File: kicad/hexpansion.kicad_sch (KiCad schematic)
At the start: 11 parts, among them J1 Hexpansion-Connector, J2 SD Card breakout, U1 AT24CS32-SSHM

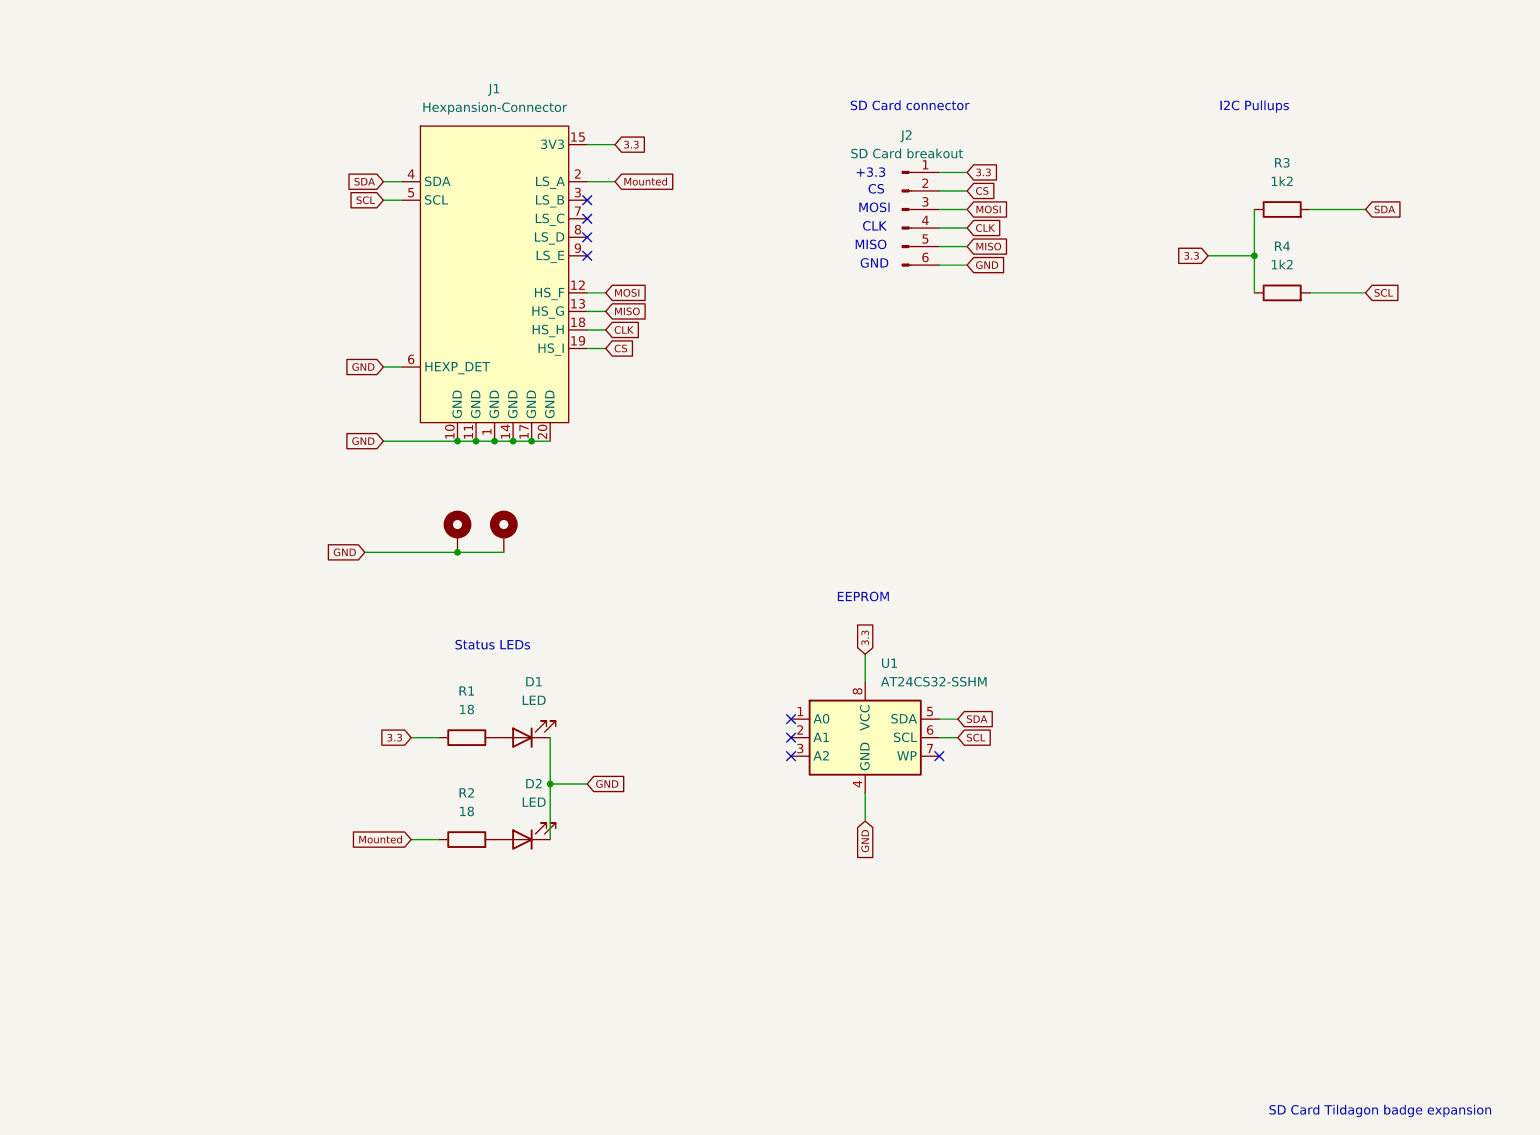
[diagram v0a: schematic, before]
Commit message: Simplify
Based on the guidelines on r/PrintedCircuitBoards I'd removed most of the
use of nets in the schematic, and added ground fills on the PCB
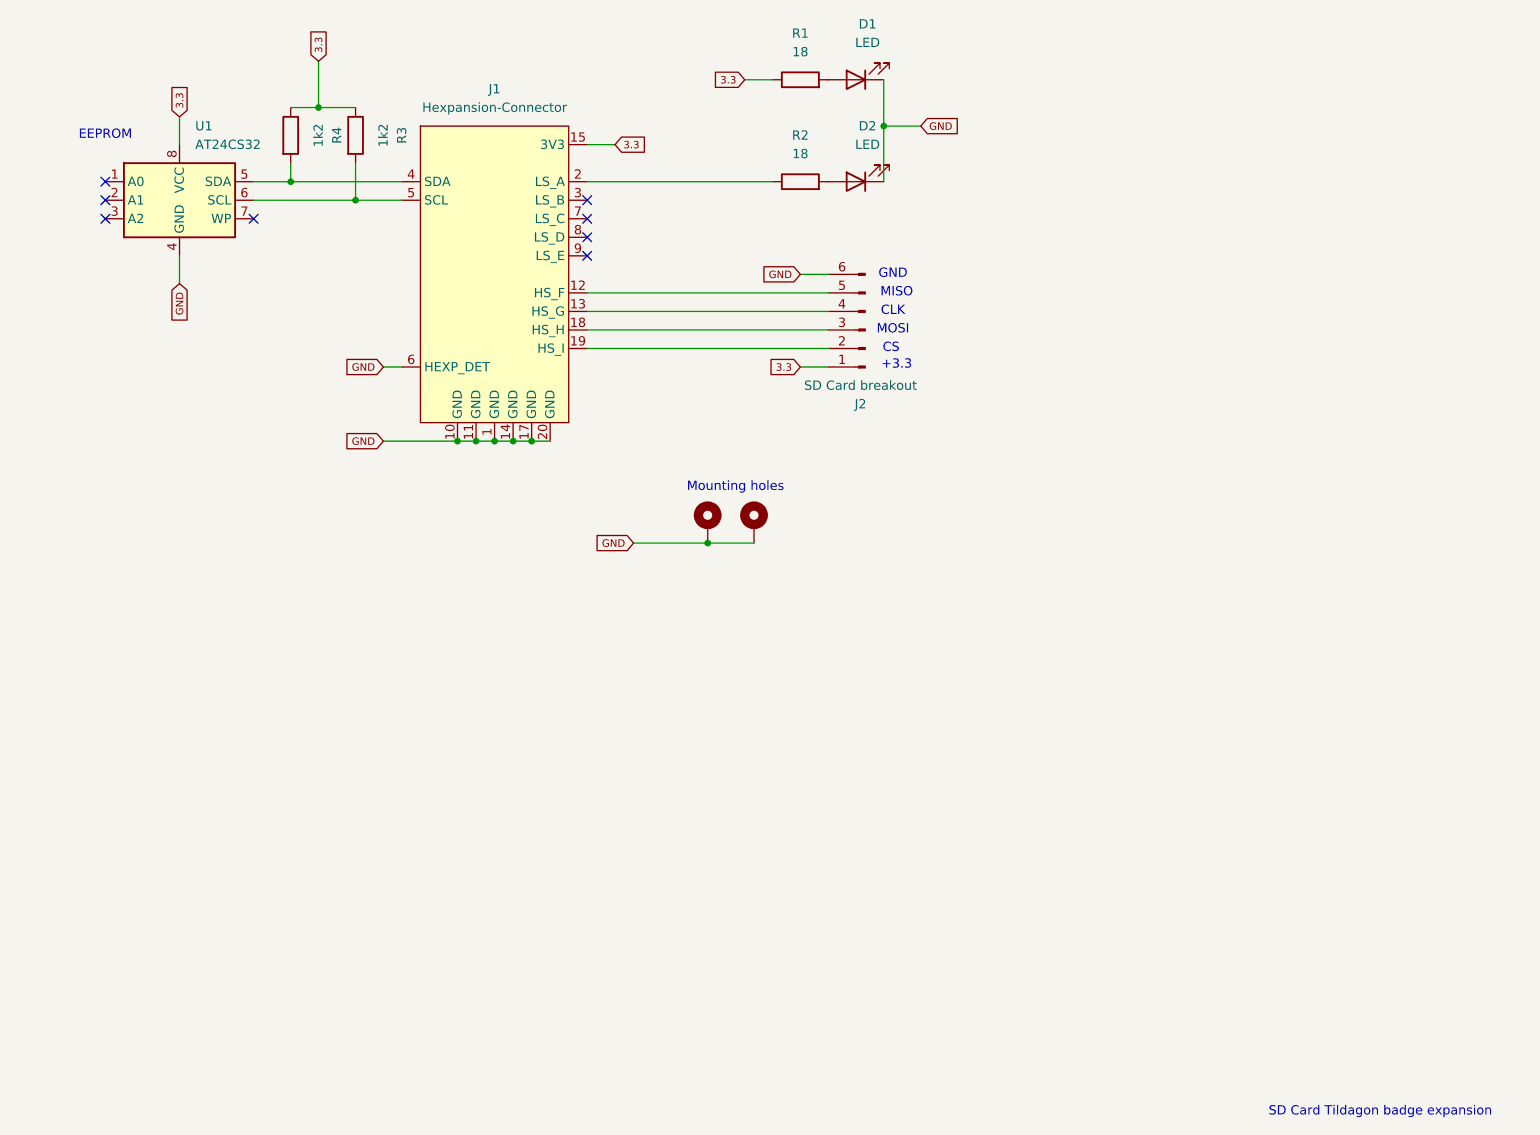
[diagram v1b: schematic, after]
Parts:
- U1: value AT24CS32-SSHM -> AT24CS32
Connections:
- net CLK: no longer names the net of J1.18 (HS_H)
- net CLK: now also J2.3 (Pin_3); no longer J2.4 (Pin_4)
- net CS: no longer names the net of J1.19 (HS_I), J2.2 (Pin_2)
- net MISO: no longer names the net of J1.13 (HS_G)
- net MISO: now also J2.4 (Pin_4); no longer J2.5 (Pin_5)
- net MOSI: no longer names the net of J1.12 (HS_F)
- net MOSI: now also J2.5 (Pin_5); no longer J2.3 (Pin_3)
- net Mounted: no longer names the net of J1.2 (LS_A), R2.1
- net SCL: no longer names the net of J1.5 (SCL), U1.6 (SCL)
- net SCL: now also R3.2; no longer R4.2
- net SDA: no longer names the net of J1.4 (SDA), U1.5 (SDA)
- net SDA: now also R4.2; no longer R3.2
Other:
- note added: "Mounting holes"
- note removed: "I2C Pullups"
- note removed: "SD Card connector"
- note removed: "Status LEDs"
- moved on the sheet: D1, D2, J2, R1, R2, R3, R4, U1

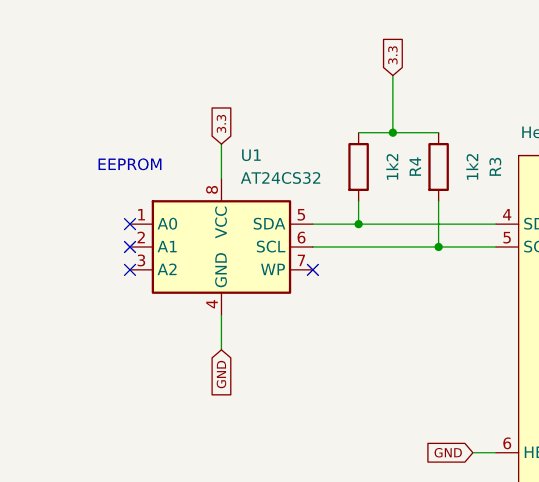
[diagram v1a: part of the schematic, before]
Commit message: Add decoupling cap
Not yet sure if I'll need it, but definitely no harm in leaving room for
a decoupling cap for the flash chip.

The SD card breakout boards already have them built in.
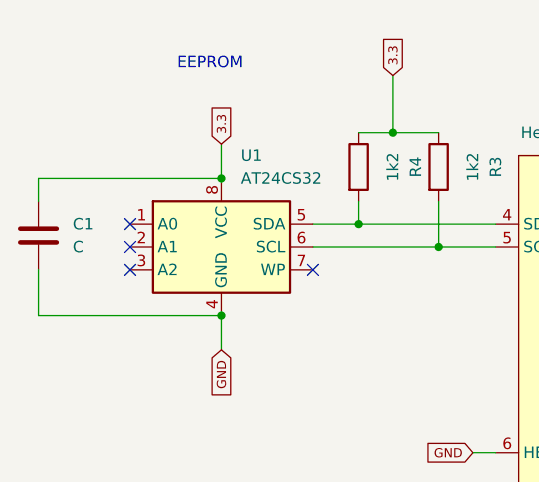
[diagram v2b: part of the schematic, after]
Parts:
- added C1: C, Capacitor_SMD:C_0603_1608Metric_Pad1.08x0.95mm_HandSolder, symbol Device:C
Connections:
- net 3.3: now also C1.2
- net GND: now also C1.1
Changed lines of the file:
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@@
 	(text "EEPROM"
 		(exclude_from_sim no)
-		(at 30.48 55.88 0)
+		(at 39.37 44.45 0)
 		(effects
 			(font
@@
 	)
 	(junction
+		(at 40.64 72.39)
+		(diameter 0)
+		(color 0 0 0 0)
+	)
+	(junction
 		(at 137.16 54.61)
 		(diameter 0)
 		(color 0 0 0 0)
 	)
+	(junction
+		(at 40.64 57.15)
+		(diameter 0)
+		(color 0 0 0 0)
+	)
 	(no_connect
 		(at 96.52 64.77)
@@
 	(wire
 		(pts
+			(xy 20.32 59.69) (xy 20.32 57.15)
+		)
+		(stroke
+			(width 0)
+			(type default)
+		)
+	)
+	(wire
+		(pts
+			(xy 137.16 54.61) (xy 137.16 62.23)
+		)
+		(stroke
+			(width 0)
+			(type default)
+		)
+	)
+	(wire
+		(pts
+			(xy 137.16 48.26) (xy 137.16 54.61)
+		)
+		(stroke
+			(width 0)
+			(type default)
+		)
+	)
+	(wire
+		(pts
+			(xy 20.32 67.31) (xy 20.32 72.39)
+		)
+		(stroke
+			(width 0)
+			(type default)
+		)
+	)
+	(wire
+		(pts
+			(xy 59.69 45.72) (xy 59.69 52.07)
+		)
+		(stroke
+			(width 0)
+			(type default)
+		)
+	)
+	(wire
+		(pts
+			(xy 55.88 52.07) (xy 59.69 52.07)
+		)
+		(stroke
+			(width 0)
+			(type default)
+		)
+	)
+	(wire
+		(pts
+			(xy 68.58 87.63) (xy 71.12 87.63)
+		)
+		(stroke
+			(width 0)
+			(type default)
+		)
+	)
+	(wire
+		(pts
+			(xy 50.8 64.77) (xy 64.77 64.77)
+		)
+		(stroke
+			(width 0)
+			(type default)
+		)
+	)
+	(wire
+		(pts
+			(xy 129.54 74.93) (xy 125.73 74.93)
+		)
+		(stroke
+			(width 0)
+			(type default)
+		)
+	)
+	(wire
+		(pts
+			(xy 96.52 57.15) (xy 100.33 57.15)
+		)
+		(stroke
+			(width 0)
+			(type default)
+		)
+	)
+	(wire
+		(pts
+			(xy 64.77 59.69) (xy 64.77 64.77)
+		)
+		(stroke
+			(width 0)
+			(type default)
+		)
+	)
+	(wire
+		(pts
+			(xy 129.54 87.63) (xy 125.73 87.63)
+		)
+		(stroke
+			(width 0)
+			(type default)
+		)
+	)
+	(wire
+		(pts
+			(xy 20.32 72.39) (xy 40.64 72.39)
+		)
+		(stroke
+			(width 0)
+			(type default)
+		)
+	)
+	(wire
+		(pts
+			(xy 50.8 62.23) (xy 55.88 62.23)
+		)
+		(stroke
+			(width 0)
+			(type default)
+		)
+	)
+	(wire
+		(pts
 			(xy 40.64 72.39) (xy 40.64 76.2)
 		)
@@
 	(wire
 		(pts
-			(xy 137.16 54.61) (xy 137.16 62.23)
-		)
-		(stroke
-			(width 0)
-			(type default)
-		)
-	)
-	(wire
-		(pts
-			(xy 137.16 48.26) (xy 137.16 54.61)
-		)
-		(stroke
-			(width 0)
-			(type default)
-		)
-	)
-	(wire
-		(pts
-			(xy 59.69 45.72) (xy 59.69 52.07)
-		)
-		(stroke
-			(width 0)
-			(type default)
-		)
-	)
-	(wire
-		(pts
-			(xy 55.88 52.07) (xy 59.69 52.07)
-		)
-		(stroke
-			(width 0)
-			(type default)
-		)
-	)
-	(wire
-		(pts
-			(xy 68.58 87.63) (xy 71.12 87.63)
-		)
-		(stroke
-			(width 0)
-			(type default)
-		)
-	)
-	(wire
-		(pts
-			(xy 50.8 64.77) (xy 64.77 64.77)
-		)
-		(stroke
-			(width 0)
-			(type default)
-		)
-	)
-	(wire
-		(pts
-			(xy 129.54 74.93) (xy 125.73 74.93)
-		)
-		(stroke
-			(width 0)
-			(type default)
-		)
-	)
-	(wire
-		(pts
-			(xy 96.52 57.15) (xy 100.33 57.15)
-		)
-		(stroke
-			(width 0)
-			(type default)
-		)
-	)
-	(wire
-		(pts
-			(xy 64.77 59.69) (xy 64.77 64.77)
-		)
-		(stroke
-			(width 0)
-			(type default)
-		)
-	)
-	(wire
-		(pts
-			(xy 129.54 87.63) (xy 125.73 87.63)
-		)
-		(stroke
-			(width 0)
-			(type default)
-		)
-	)
-	(wire
-		(pts
-			(xy 50.8 62.23) (xy 55.88 62.23)
-		)
-		(stroke
-			(width 0)
-			(type default)
-		)
-	)
-	(wire
-		(pts
 			(xy 40.64 53.34) (xy 40.64 57.15)
+		)
+		(stroke
+			(width 0)
+			(type default)
+		)
+	)
+	(wire
+		(pts
+			(xy 20.32 57.15) (xy 40.64 57.15)
 		)
 		(stroke
@@
 					(unit 1)
 				)
+			)
+		)
+	)
+	(symbol
+		(lib_id "Device:C")
+		(at 20.32 63.5 180)
+		(unit 1)
+		(exclude_from_sim no)
+		(in_bom yes)
+		(on_board yes)
+		(dnp no)
+		(fields_autoplaced yes)
+		(property "Reference" "C1"
+			(at 24.13 62.2299 0)
+			(effects
+				(font
+					(size 1.27 1.27)
+				)
+				(justify right)
+			)
+		)
+		(property "Value" "C"
+			(at 24.13 64.7699 0)
+			(effects
+				(font
+					(size 1.27 1.27)
+				)
+				(justify right)
+			)
+		)
+		(property "Footprint" "Capacitor_SMD:C_0603_1608Metric_Pad1.08x0.95mm_HandSolder"
+			(at 19.3548 59.69 0)
+			(effects
+				(font
+					(size 1.27 1.27)
+				)
+				(hide yes)
+			)
+		)
+		(property "Datasheet" "~"
+			(at 20.32 63.5 0)
+			(effects
+				(font
+					(size 1.27 1.27)
+				)
+				(hide yes)
+			)
+		)
+		(property "Description" "Unpolarized capacitor"
+			(at 20.32 63.5 0)
+			(effects
+				(font
+					(size 1.27 1.27)
+				)
+				(hide yes)
+			)
+		)
+		(pin "1"
+		)
+		(pin "2"
+		)
+		(instances
+			(project ""
+				(path "/fb9bfa6e-c44d-469c-aa90-8ec28bcdf17f"
+					(reference "C1")
+					(unit 1)
+				)

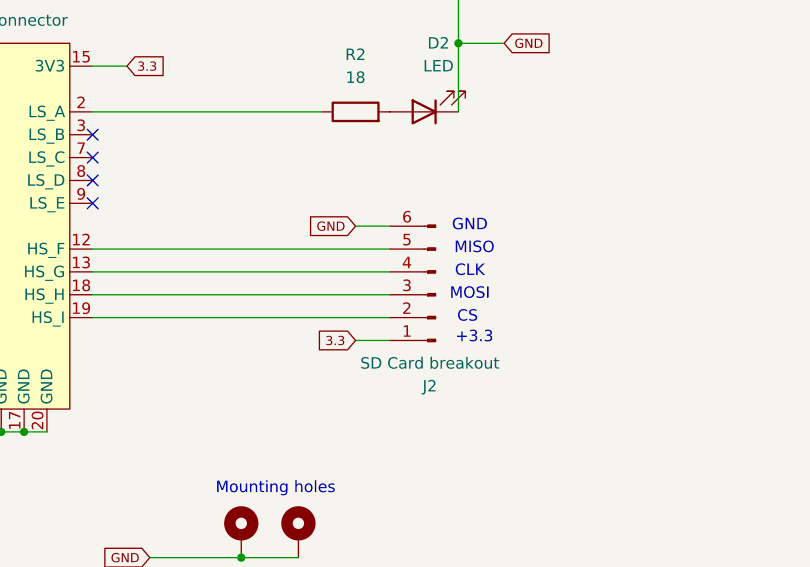
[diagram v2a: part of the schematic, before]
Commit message: Reorder GPIOs to simplify layout
Reordering the highspeed GPIOs made the SPI routing dead simple.
Reworked the rest of the board around that.
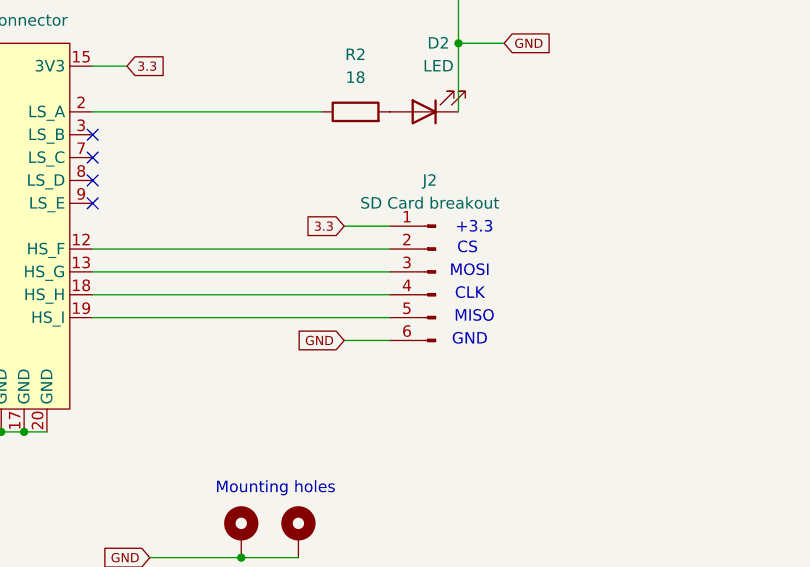
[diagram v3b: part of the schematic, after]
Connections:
- net at J2.2 (Pin_2): now also J1.12 (HS_F); no longer J1.19 (HS_I)
- net at J2.3 (Pin_3): now also J1.13 (HS_G); no longer J1.18 (HS_H)
- net at J2.4 (Pin_4): now also J1.18 (HS_H); no longer J1.13 (HS_G)
- net at J2.5 (Pin_5): now also J1.19 (HS_I); no longer J1.12 (HS_F)
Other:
- moved on the sheet: J2
